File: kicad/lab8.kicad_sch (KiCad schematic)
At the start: 44 parts, among them Q1 LTR3208E, SW1 Reset, U2 74xxx244, U3 MCP6294, U4 PIC32MX170F256B, U5 LM339AN

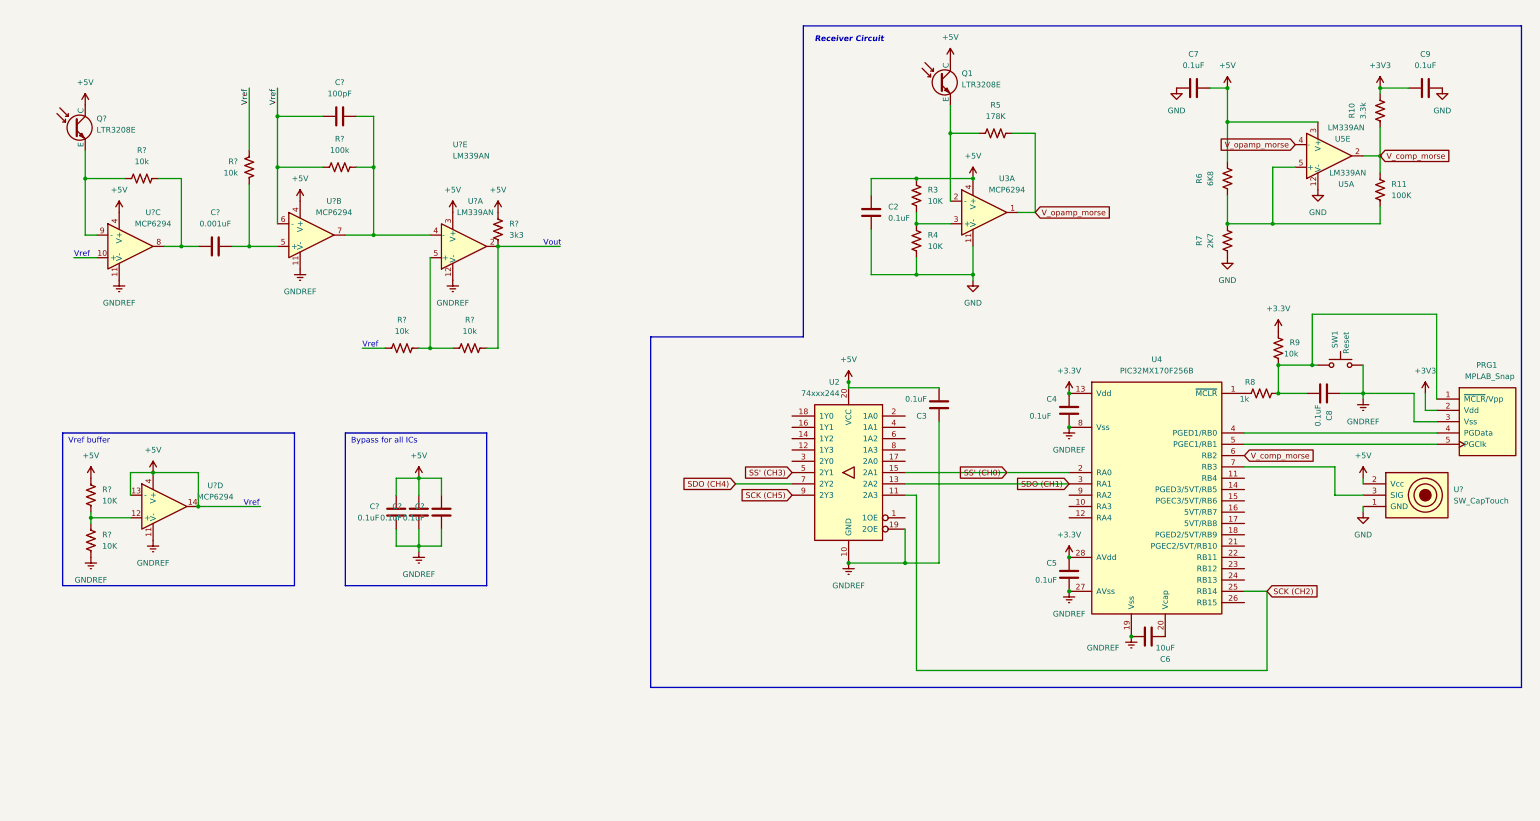
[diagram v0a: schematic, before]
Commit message: Add motors and set optical sensor pin in KiCad
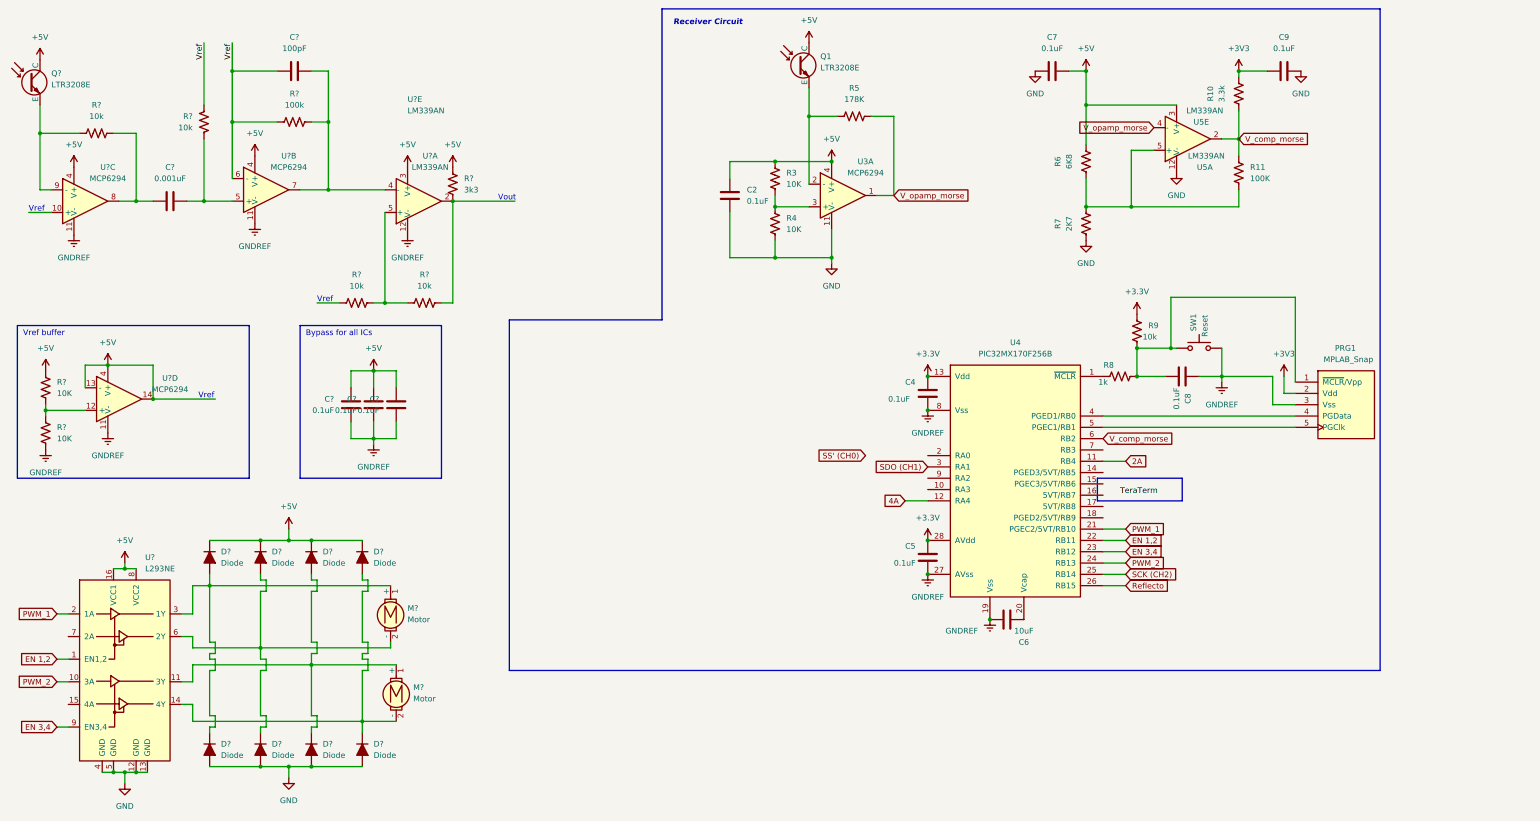
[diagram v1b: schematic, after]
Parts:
- removed C3: 0.1uF, symbol ME218_BaseLib:Cap
- removed U2: 74xxx244, symbol ME218_BaseLib:74xxx244
- removed U?: SW_CapTouch, symbol ME218_BaseLib:SW_CapTouch
- added D? (x8): Diode, symbol 218 spdl:Diode
- added M? (x2): Motor, symbol 218 spdl:Motor
- added U?: L293NE, Package_DIP:DIP-16_W7.62mm, symbol 218 spdl:L293NE
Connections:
- net +5V: now also D?.1 (K), D?.1 (K), D?.1 (K), D?.1 (K), U?.16 (VCC1), U?.8 (VCC2)
- net GND: now also D?.2 (A), D?.2 (A), D?.2 (A), D?.2 (A), U?.12 (GND), U?.13 (GND), U?.4 (GND), U?.5 (GND)
- net SS' (CH0): no longer U4.2 (RA0)
- net 2A: now reaches U4.11 (RB4)
- net 4A: now reaches U4.12 (RA4)
- net PWM_1: now reaches U4.21 (PGEC2/5VT/RB10)
- net PWM_1: now also U?.2 (1A)
- net EN 1,2: now reaches U4.22 (RB11)
- net EN 1,2: now also U?.1 (EN1,2)
- net EN 3,4: now reaches U4.23 (RB12)
- net EN 3,4: now also U?.9 (EN3,4)
- net PWM_2: now reaches U4.24 (RB13)
- net PWM_2: now also U?.10 (3A)
- net Reflecto: now reaches U4.26 (RB15)
- new net: D?.1 (K), D?.2 (A), M?.2 (-), U?.6 (2Y)
- new net: D?.1 (K), D?.2 (A), M?.2 (-), U?.14 (4Y)
- new net: D?.1 (K), D?.2 (A), M?.1 (+), U?.11 (3Y)
- new net: D?.1 (K), D?.2 (A), M?.1 (+), U?.3 (1Y)
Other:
- moved on the sheet: C2, C4, C5, C6, C7, C8, C9, C?, PRG1, Q1, Q?, R10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
